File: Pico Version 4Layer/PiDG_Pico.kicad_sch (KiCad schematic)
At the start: 44 parts, among them J1 Conn_02x05_Odd_Even, J10 Trig, J11 Laser Enable, J12 Pixel Reset, J14 Pico Socket A, J15 Pico Socket B, J16 Laser En/PWM Trig/GND, J2 Conn_02x05_Odd_Even, J3 Conn_02x05_Odd_Even, J4 Conn_02x05_Odd_Even, J5 Conn_02x05_Odd_Even, J6 Conn_02x05_Odd_Even, J7 Laser 1, J8 Laser 2, U1 74LVC1G04, U10 74LVC1G08, U11 Raspberry Pi Pico 2 W, U12 74LVC1G08, U13 UCC27524, U2 SN74LVC04AD, U3 74LVC1G04, U4 SN74LVC04AD, U5 74LVC1G04, U6 SN74LVC04AD, U7 74LVC1G08, U8 74LVC1G08, U9 NCP718xSN180

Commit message: Error free board
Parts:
- removed U9: NCP718xSN180, Package_TO_SOT_SMD:SOT-23-5, symbol Regulator_Linear:NCP718xSN180
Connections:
- net +1V8 is gone; now on net +3V3: C1.1, C2.1, C3.1, C7.1, U1.5 (VCC), U2.14 (VCC), U3.5 (VCC), U4.14 (VCC), U5.5 (VCC), U6.14 (VCC)
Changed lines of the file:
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@@
 	)
 	(junction
-		(at 40.64 208.28)
-		(diameter 0)
-		(color 0 0 0 0)
-	)
-	(junction
 		(at 72.39 97.79)
 		(diameter 0)
@@
 	)
 	(junction
-		(at 59.69 208.28)
-		(diameter 0)
-		(color 0 0 0 0)
-	)
-	(junction
 		(at 356.87 78.74)
 		(diameter 0)
@@
 	(wire
 		(pts
-			(xy 40.64 208.28) (xy 40.64 210.82)
-		)
-		(stroke
-			(width 0)
-			(type default)
-		)
-	)
-	(wire
-		(pts
 			(xy 210.82 34.29) (xy 213.36 34.29)
 		)
@@
 	(wire
 		(pts
-			(xy 59.69 208.28) (xy 55.88 208.28)
-		)
-		(stroke
-			(width 0)
-			(type default)
-		)
-	)
-	(wire
-		(pts
 			(xy 242.57 31.75) (xy 236.22 31.75)
 		)
@@
 	)
 	(symbol
-		(lib_id "power:+1V8")
+		(lib_id "power:+3V3")
 		(at 59.69 208.28 0)
 		(unit 1)
@@
 			)
 		)
-		(property "Value" "+1V8"
+		(property "Value" "+3V3"
 			(at 59.69 203.2 0)
 			(effects
@@
 	)
 	(symbol
-		(lib_id "power:+1V8")
+		(lib_id "power:+3V3")
 		(at 86.36 119.38 0)
 		(unit 1)
@@
 			)
 		)
-		(property "Value" "+1V8"
+		(property "Value" "+3V3"
 			(at 89.662 119.126 0)
 			(effects
@@
 	)
 	(symbol
-		(lib_id "Regulator_Linear:NCP718xSN180")
-		(at 48.26 210.82 0)
-		(unit 1)
-		(exclude_from_sim no)
-		(in_bom yes)
-		(on_board yes)
-		(dnp no)
-		(fields_autoplaced yes)
-		(property "Reference" "U9"
-			(at 48.26 200.66 0)
-			(effects
-				(font
-					(size 1.27 1.27)
-				)
-			)
-		)
-		(property "Value" "NCP718xSN180"
-			(at 48.26 203.2 0)
-			(effects
-				(font
-					(size 1.27 1.27)
-				)
-			)
-		)
-		(property "Footprint" "Package_TO_SOT_SMD:SOT-23-5"
-			(at 48.26 201.93 0)
-			(effects
-				(font
-					(size 1.27 1.27)
-				)
-				(hide yes)
-			)
-		)
-		(property "Datasheet" "https://www.onsemi.com/pub/Collateral/NCP718-D.PDF"
-			(at 48.26 198.12 0)
-			(effects
-				(font
-					(size 1.27 1.27)
-				)
-				(hide yes)
-			)
-		)
-		(property "Description" "300-mA, Wide Input Voltage, Low-IQ LDO, 1.8V, SOT-23"
-			(at 48.26 210.82 0)
-			(effects
-				(font
-					(size 1.27 1.27)
-				)
-				(hide yes)
-			)
-		)
-		(pin "5"
-		)
-		(pin "1"
-		)
-		(pin "3"
-		)
-		(pin "2"
-		)
-		(pin "4"
-		)
-		(instances
-			(project ""
-				(path "/e63e39d7-6ac0-4ffd-8aa3-1841a4541b55"
-					(reference "U9")
-					(unit 1)
-				)
-			)
-		)
-	)
-	(symbol
-		(lib_id "power:+1V8")
+		(lib_id "power:+3V3")
 		(at 86.36 77.47 0)
 		(unit 1)
@@
 			)
 		)
-		(property "Value" "+1V8"
+		(property "Value" "+3V3"
 			(at 86.36 72.39 0)
 			(effects
@@
 	)
 	(symbol
-		(lib_id "power:+1V8")
+		(lib_id "power:+3V3")
 		(at 86.36 31.75 0)
 		(unit 1)
@@
 			)
 		)
-		(property "Value" "+1V8"
+		(property "Value" "+3V3"
 			(at 86.36 26.67 0)
 			(effects
@@
 			)
 		)
-		(property "Value" "+1V8"
+		(property "Value" "+3V3"
 			(at 38.1 228.6 0)
 			(effects

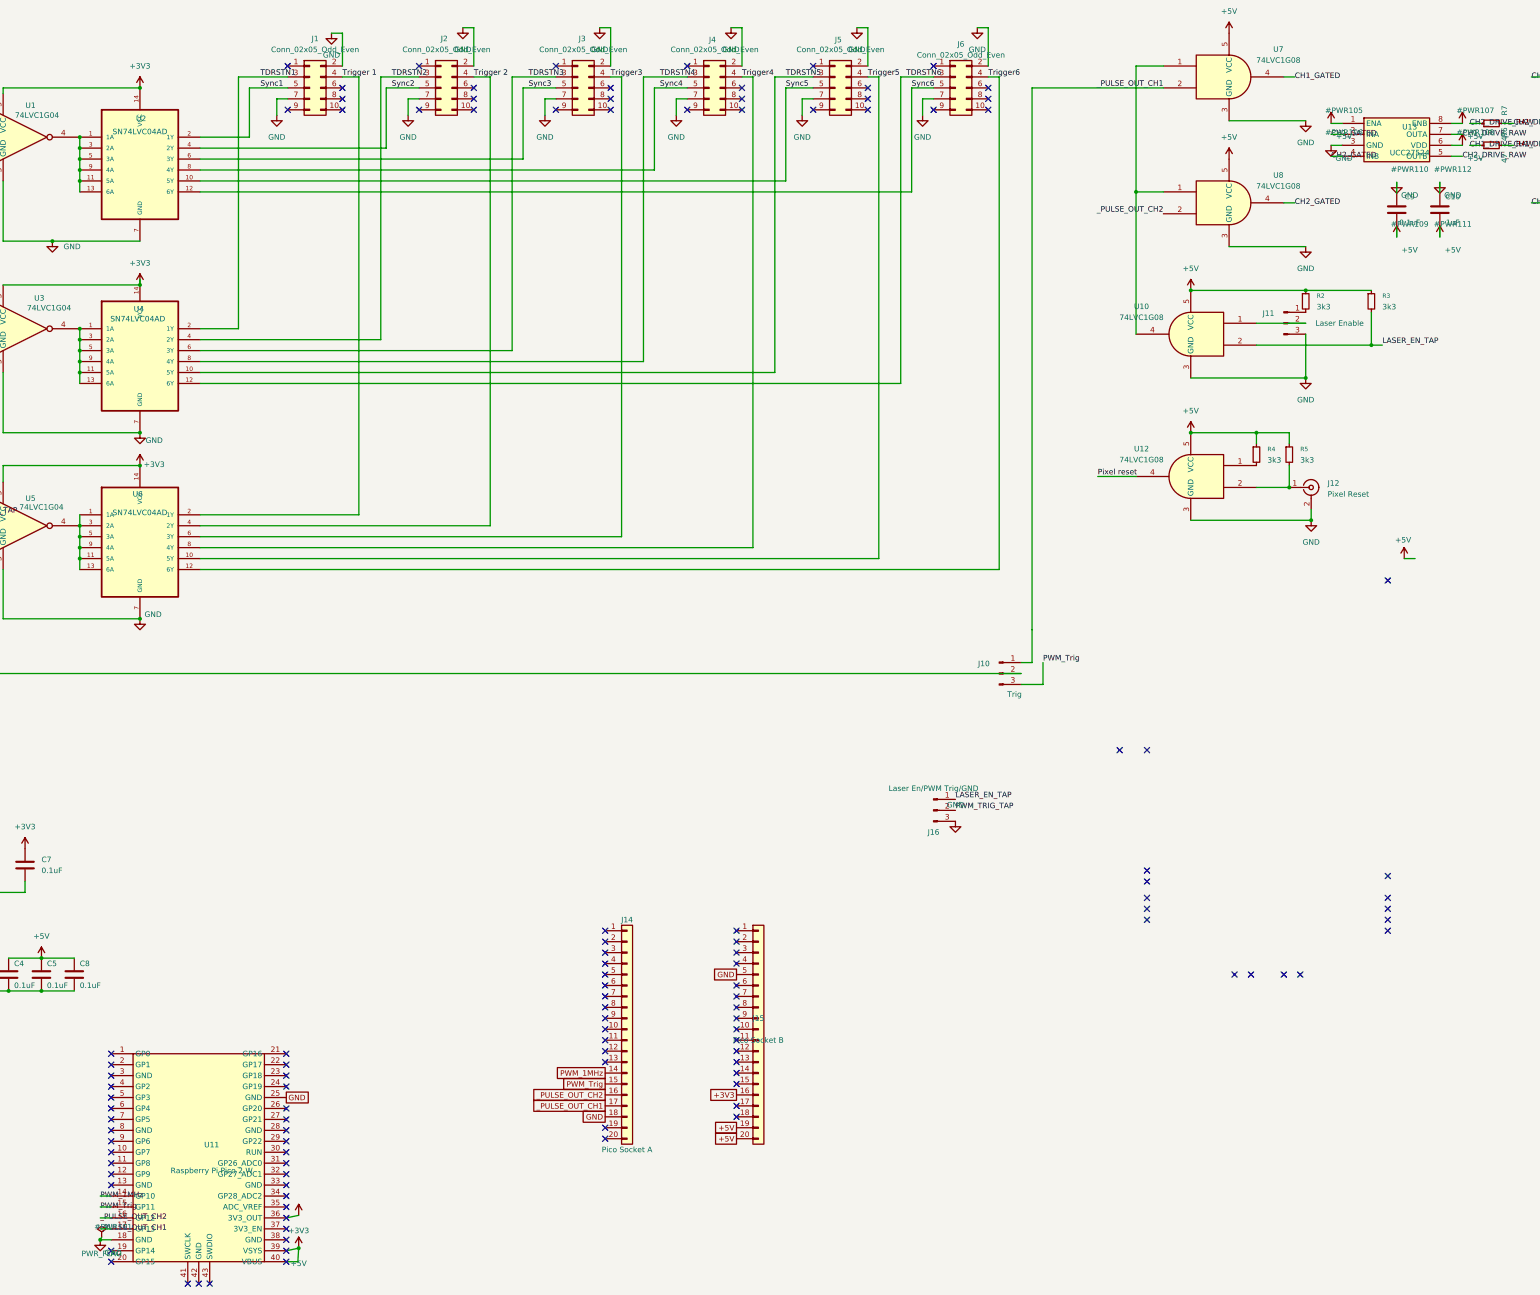
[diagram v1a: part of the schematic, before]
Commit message: A few manual tweaks to MHz output pin location
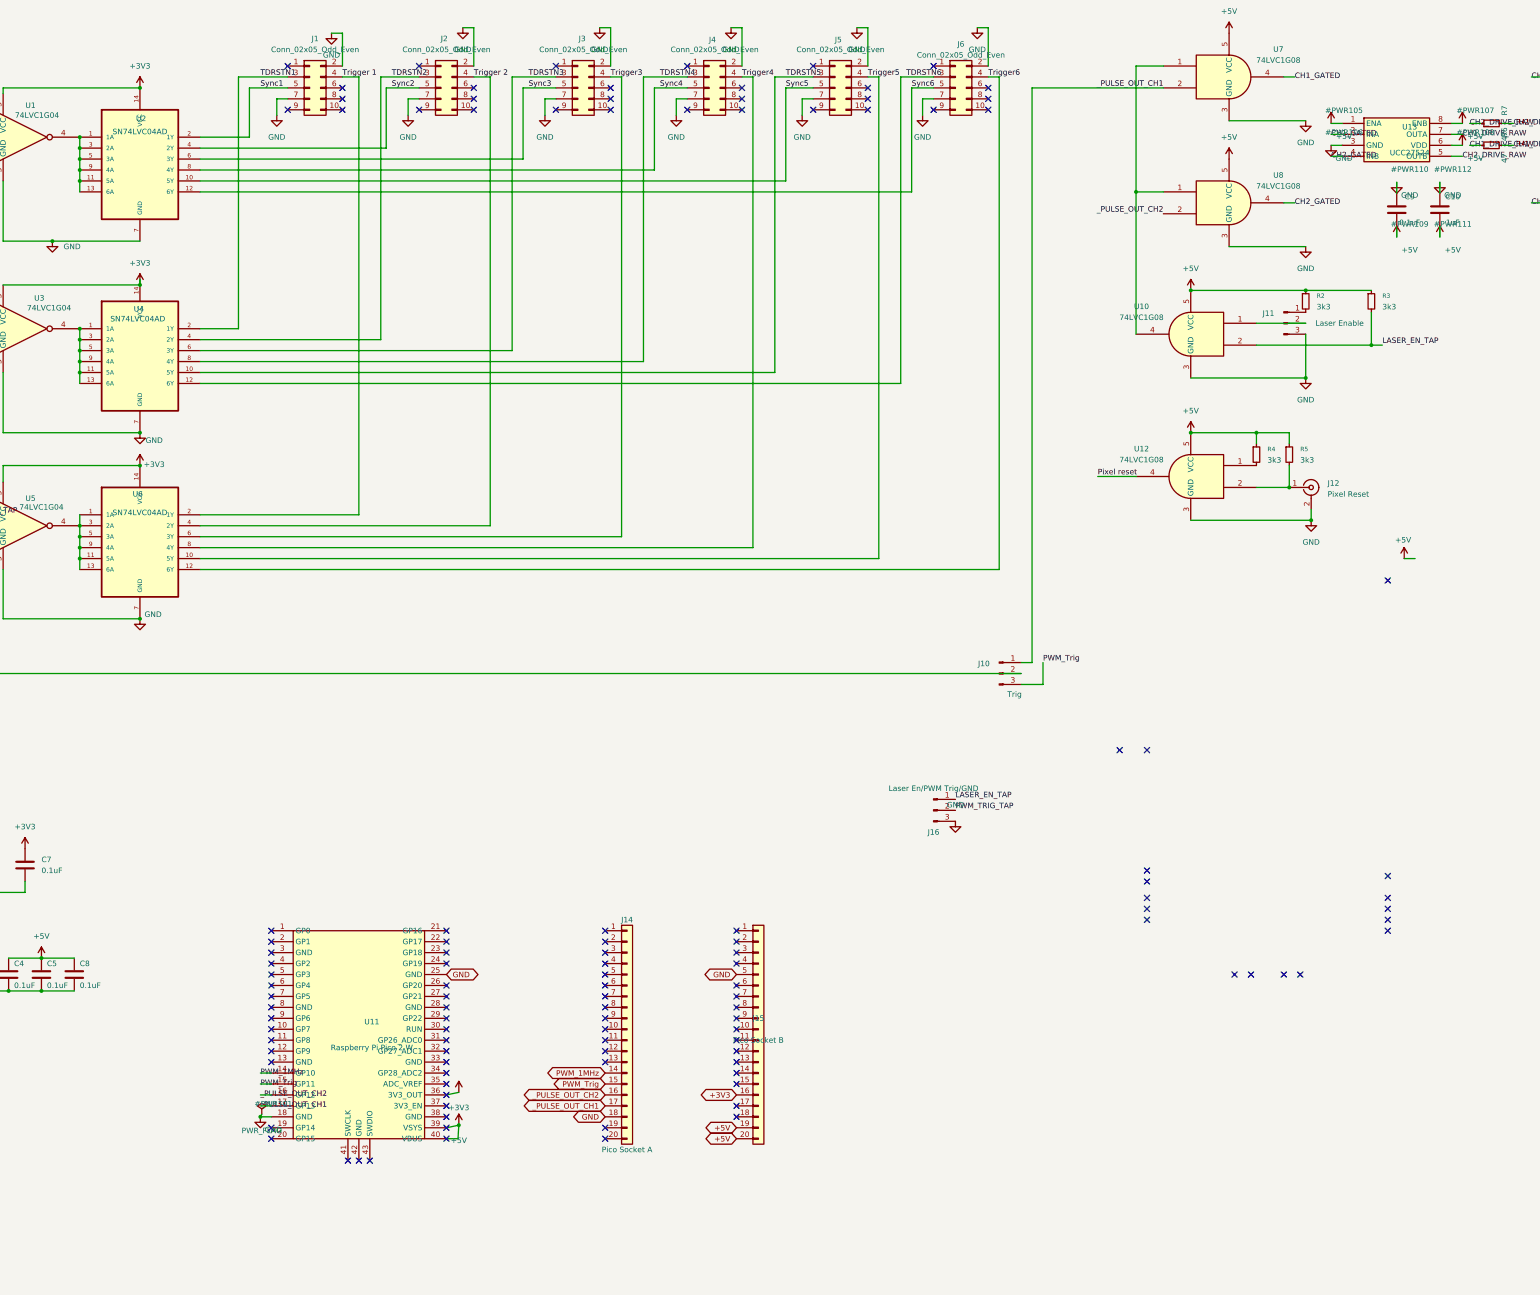
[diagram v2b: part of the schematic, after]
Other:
- moved on the sheet: U11

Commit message: Refined and ready version
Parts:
- removed TP3: 1MHz sync, Connector_PinHeader_2.54mm:PinHeader_1x01_P2.54mm_Horizontal, symbol Connector:TestPoint
- added TP3: 1MHz sync + GND, Connector_PinHeader_2.54mm:PinHeader_1x02_P2.54mm_Horizontal, symbol Connector:Conn_01x02_Pin
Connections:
- net GND: now also TP3.2 (Pin_2)
- net PWM_1MHz: now also TP3.1 (Pin_1)
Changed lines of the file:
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@@
 	(wire
 		(pts
-			(xy 21.59 43.18) (xy 44.45 43.18)
+			(xy 26.67 43.18) (xy 29.21 43.18)
+		)
+		(stroke
+			(width 0)
+			(type default)
+		)
+	)
+	(wire
+		(pts
+			(xy 29.21 43.18) (xy 44.45 43.18)
 		)
 		(stroke
@@
 	)
 	(symbol
-		(lib_id "Connector:TestPoint")
-		(at 21.59 43.18 0)
-		(unit 1)
-		(body_style 1)
-		(exclude_from_sim no)
-		(in_bom yes)
-		(on_board yes)
-		(in_pos_files yes)
-		(dnp no)
-		(fields_autoplaced yes)
-		(property "Reference" "TP3"
-			(at 24.13 38.6079 0)
-			(show_name no)
-			(do_not_autoplace no)
-			(effects
-				(font
-					(size 1.27 1.27)
-				)
-				(justify left)
-			)
-		)
-		(property "Value" "1MHz sync"
-			(at 24.13 41.1479 0)
-			(show_name no)
-			(do_not_autoplace no)
-			(effects
-				(font
-					(size 1.27 1.27)
-				)
-				(justify left)
-			)
-		)
-		(property "Footprint" "Connector_PinHeader_2.54mm:PinHeader_1x01_P2.54mm_Horizontal"
-			(at 26.67 43.18 0)
-			(hide yes)
-			(show_name no)
-			(do_not_autoplace no)
-			(effects
-				(font
-					(size 1.27 1.27)
-				)
-			)
-		)
-		(property "Datasheet" ""
-			(at 26.67 43.18 0)
-			(hide yes)
-			(show_name no)
-			(do_not_autoplace no)
-			(effects
-				(font
-					(size 1.27 1.27)
-				)
-			)
-		)
-		(property "Description" "test point"
-			(at 21.59 43.18 0)
-			(hide yes)
-			(show_name no)
-			(do_not_autoplace no)
-			(effects
-				(font
-					(size 1.27 1.27)
-				)
-			)
-		)
-		(pin "1"
-		)
-		(instances
-			(project "PiDG_Pico"
-				(path "/e63e39d7-6ac0-4ffd-8aa3-1841a4541b55"
-					(reference "TP3")
-					(unit 1)
-				)
-			)
-		)
-	)
-	(symbol
 		(lib_id "power:GND")
 		(at 50.8 241.3 0)
@@
 		)
 	)
+	(symbol
+		(lib_id "Connector:Conn_01x02_Pin")
+		(at 21.59 43.18 0)
+		(unit 1)
+		(body_style 1)
+		(exclude_from_sim no)
+		(in_bom yes)
+		(on_board yes)
+		(in_pos_files yes)
+		(dnp no)
+		(property "Reference" "TP3"
+			(at 21.59 45.72 0)
+			(show_name no)
+			(do_not_autoplace no)
+			(effects
+				(font
+					(size 1.27 1.27)
+				)
+			)
+		)
+		(property "Value" "1MHz sync + GND"
+			(at 21.59 38.1 0)
+			(show_name no)
+			(do_not_autoplace no)
+			(effects
+				(font
+					(size 1.27 1.27)
+				)
+			)
+		)
+		(property "Footprint" "Connector_PinHeader_2.54mm:PinHeader_1x02_P2.54mm_Horizontal"
+			(at 21.59 43.18 0)
+			(hide yes)
+			(show_name no)
+			(do_not_autoplace no)
+			(effects
+				(font
+					(size 1.27 1.27)
+				)
+			)
+		)
+		(property "Datasheet" ""
+			(at 21.59 43.18 0)
+			(hide yes)
+			(show_name no)
+			(do_not_autoplace no)
+			(effects
+				(font
+					(size 1.27 1.27)
+				)
+			)
+		)
+		(property "Description" "test point"
+			(at 21.59 43.18 0)
+			(hide yes)
+			(show_name no)
+			(do_not_autoplace no)
+			(effects
+				(font
+					(size 1.27 1.27)
+				)
+			)
+		)
+		(pin "1"
+		)
+		(pin "2"
+		)
+		(instances
+			(project "PiDG_Pico"
+				(path "/e63e39d7-6ac0-4ffd-8aa3-1841a4541b55"
+					(reference "TP3")
+					(unit 1)
+				)
+			)
+		)
+	)
+	(wire
+		(pts
+			(xy 26.67 43.18) (xy 29.21 43.18)
+		)
+		(stroke
+			(width 0)
+			(type default)
+		)
+	)
+	(junction
+		(at 26.67 43.18)
+		(diameter 0)
+		(color 0 0 0 0)
+	)
+	(junction
+		(at 29.21 43.18)
+		(diameter 0)
+		(color 0 0 0 0)
+	)
+	(label "PWM_1MHz"
+		(at 29.21 43.18 0)
+		(effects
+			(font
+				(size 1.27 1.27)
+			)
+			(justify left bottom)
+		)
+	)
+	(wire
+		(pts
+			(xy 26.67 45.72) (xy 29.21 45.72)
+		)
+		(stroke
+			(width 0)
+			(type default)
+		)
+	)
+	(label "GND"
+		(at 29.21 45.72 0)
+		(effects
+			(font
+				(size 1.27 1.27)
+			)
+			(justify left bottom)
+		)
+	)
